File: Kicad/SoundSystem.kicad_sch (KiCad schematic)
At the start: 3 parts, among them J10 Sub OUT, J11 Right OUT, J12 Left OUT

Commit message: subwoofer fix
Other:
- moved on the sheet: J10, J11, J12

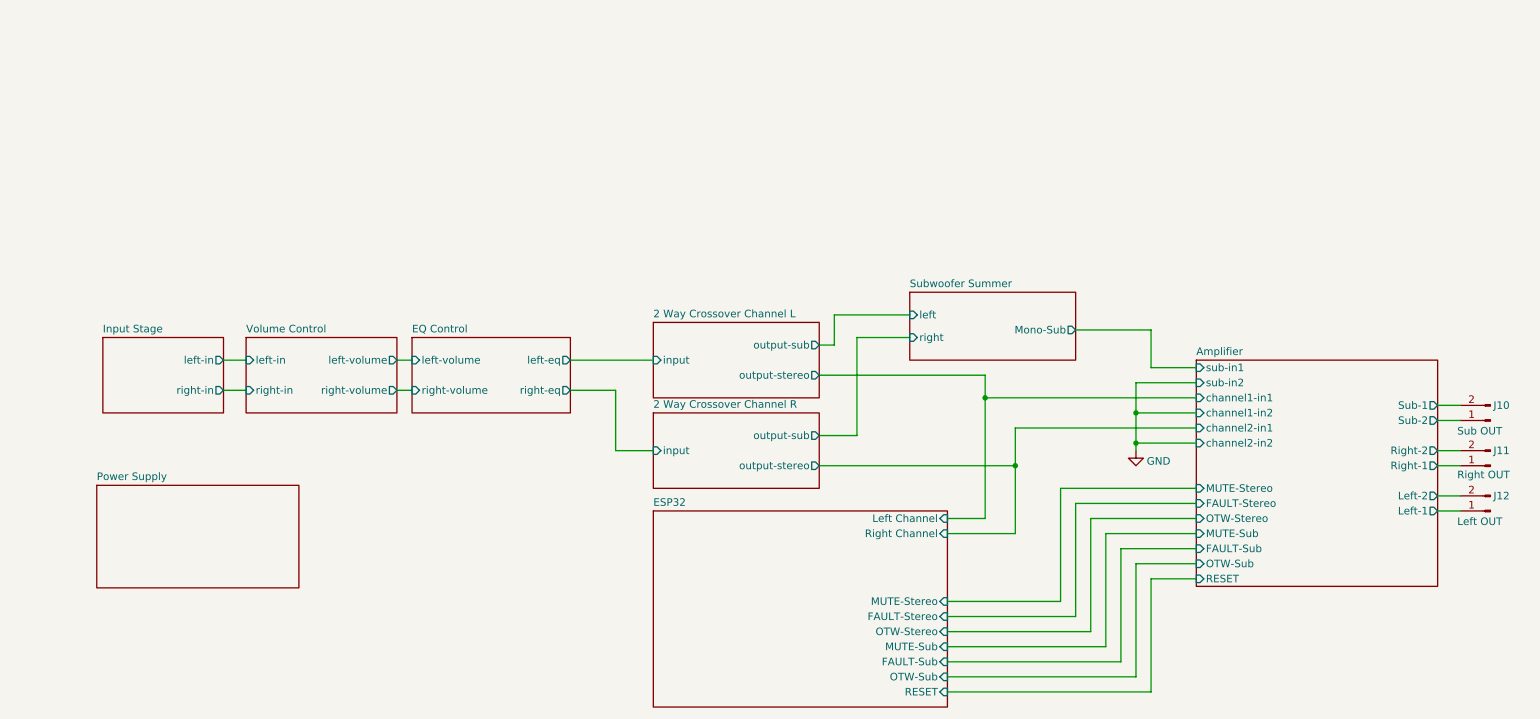
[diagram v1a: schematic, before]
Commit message: moved dac to input path and added input multiplexing
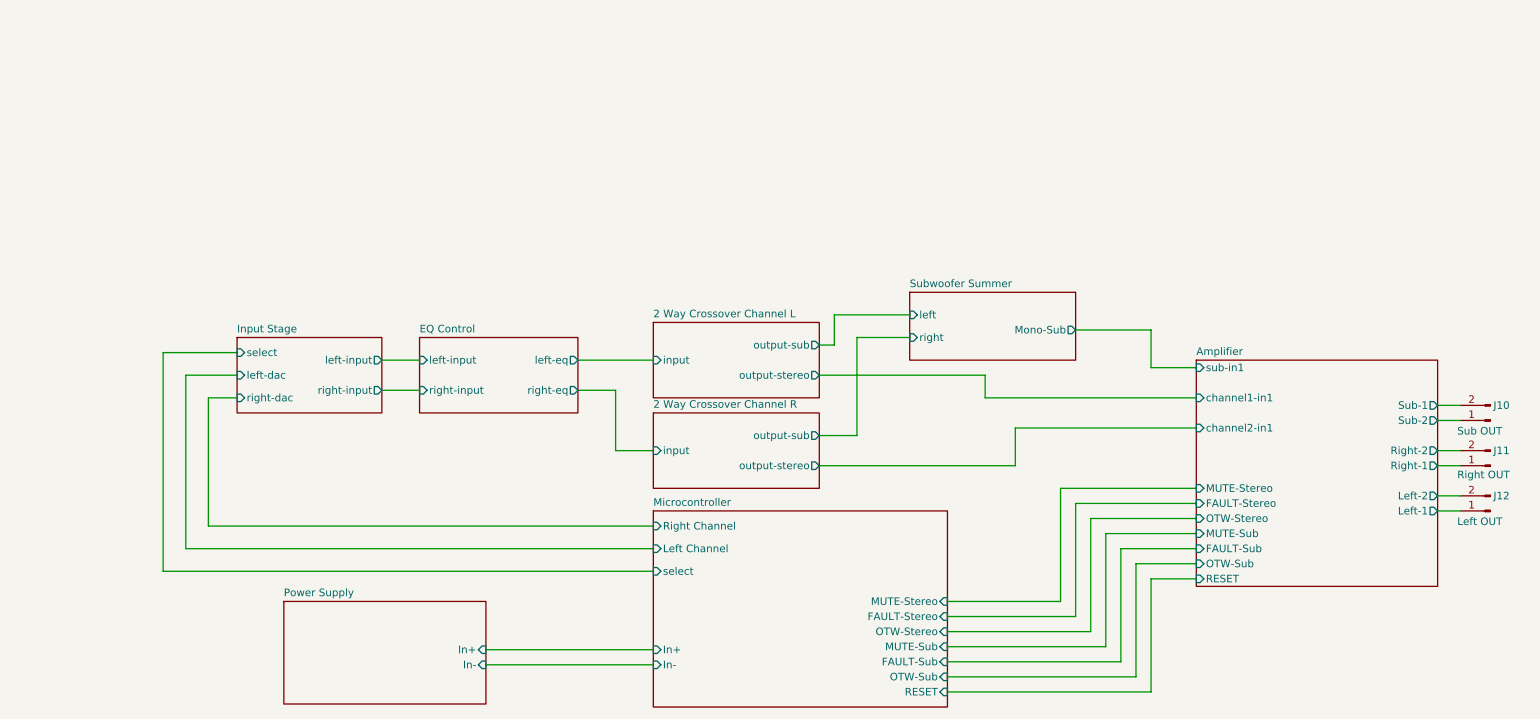
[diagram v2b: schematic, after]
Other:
- sheet ESP32 renamed Microcontroller
- removed sheet Volume Control
- sheet Amplifier ports: added none; removed channel1-in2, channel2-in2, sub-in2
- sheet EQ Control ports: added left-input, right-input; removed left-volume, right-volume
- sheet Input Stage ports: added left-dac, left-input, right-dac, right-input, select; removed left-in, right-in
- sheet Microcontroller ports: added In+, In-, select; removed none
- sheet Power Supply ports: added In+, In-; removed none
